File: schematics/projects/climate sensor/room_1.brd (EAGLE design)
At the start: 100 x 80 mm, 8 parts

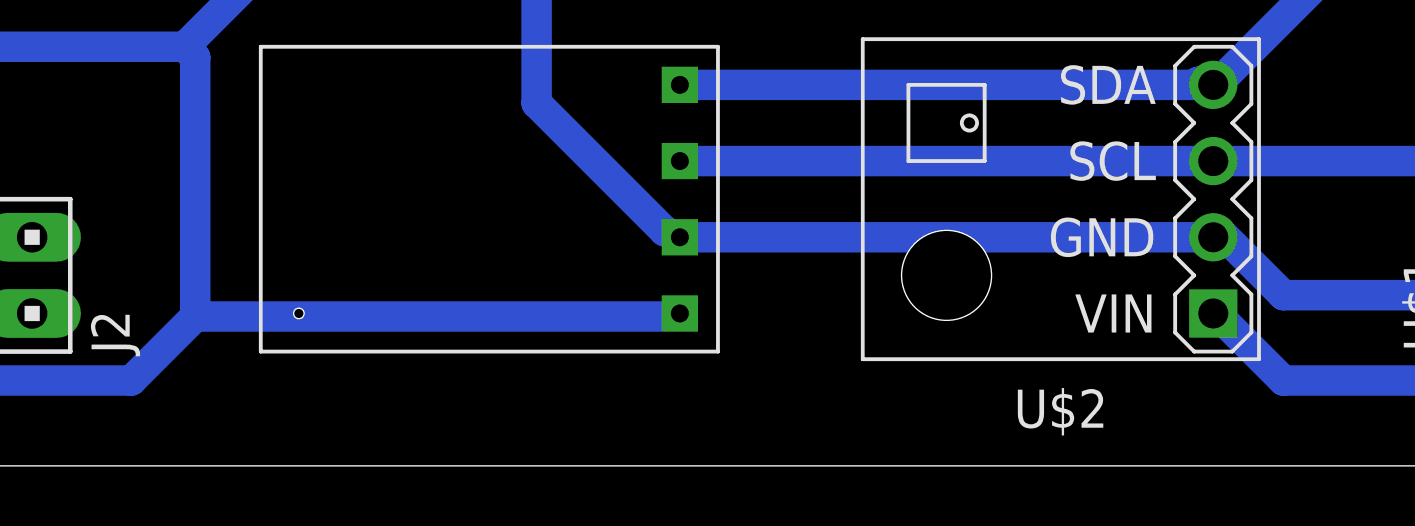
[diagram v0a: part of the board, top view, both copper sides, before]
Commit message: added eagle board files for low-voltage schemas
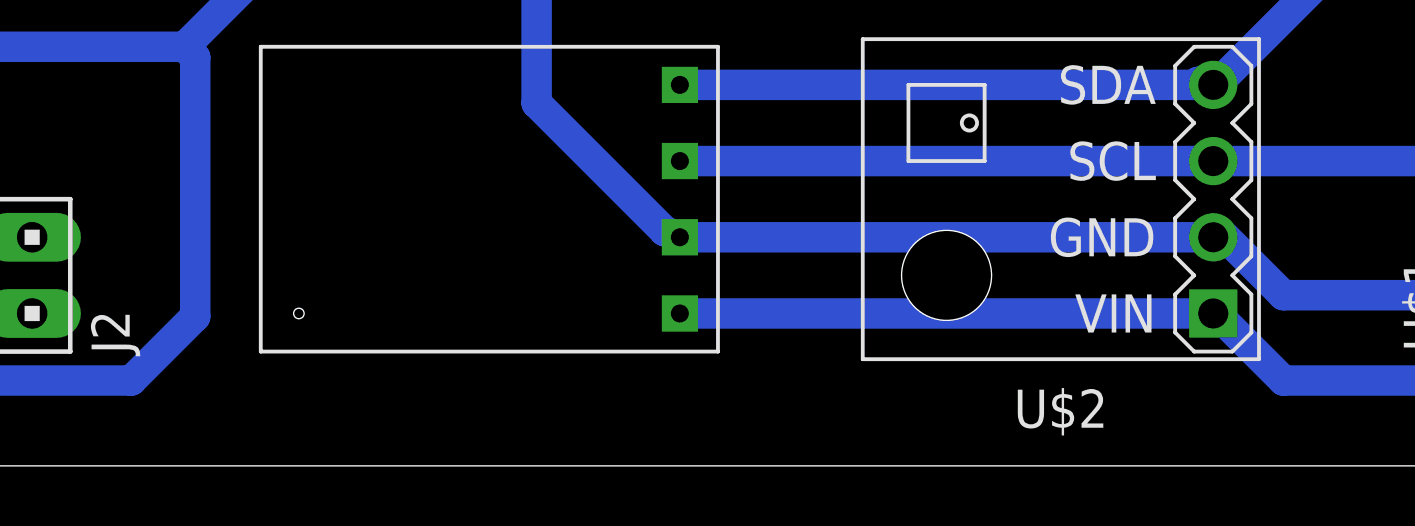
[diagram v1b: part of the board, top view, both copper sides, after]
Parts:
- renumbered GY_SGP1 to GY_SGP30_1
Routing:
- net 3V3: track 114.2 -> 132.2 mm
- net +5V: track 241.8 -> 226.2 mm
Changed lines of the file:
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@@
 <elements>
 <element name="C1" library="my_devices" package="C" value="1000 mF" x="13.97" y="6.35" smashed="yes" rot="R270"/>
-<element name="GY_SGP1" library="my_devices" package="GY-SGP30" value="GY-SGP30" x="43.18" y="8.89" smashed="yes" rot="R180"/>
+<element name="GY_SGP30_1" library="my_devices" package="GY-SGP30" value="GY-SGP30" x="43.18" y="8.89" smashed="yes" rot="R180"/>
 <element name="J2" library="con-amp" library_urn="urn:adsk.eagle:library:127" package="10X02MTA" package3d_urn="urn:adsk.eagle:package:8081649/1" value="" x="21.59" y="6.35" smashed="yes" rot="R90">
 <attribute name="NAME" x="24.8412" y="3.7338" size="1.27" layer="25" rot="R90"/>
@@
 <contactref element="U$3" pad="GND"/>
 <contactref element="U$3" pad="GND_1"/>
-<contactref element="GY_SGP1" pad="GND"/>
+<contactref element="GY_SGP30_1" pad="GND"/>
 <contactref element="U$11" pad="GND"/>
 <contactref element="U$2" pad="2"/>
@@
 <wire x1="93.8784" y1="51.2064" x2="93.97" y2="50.79" width="1.016" layer="16"/>
 <wire x1="27.0256" y1="4.9784" x2="24.892" y2="2.8448" width="1.016" layer="16"/>
-<wire x1="42.672" y1="4.9784" x2="27.0256" y2="4.9784" width="1.016" layer="16"/>
 <wire x1="9.2456" y1="13.97" x2="26.67" y2="13.97" width="1.016" layer="16"/>
 <wire x1="26.67" y1="13.97" x2="27.0256" y2="13.6144" width="1.016" layer="16"/>
@@
 <signal name="I2C_SCL">
 <contactref element="U$1" pad="36"/>
-<contactref element="GY_SGP1" pad="SCL"/>
+<contactref element="GY_SGP30_1" pad="SCL"/>
 <contactref element="U$2" pad="3"/>
 <wire x1="43.18" y1="10.16" x2="60.96" y2="10.16" width="1.016" layer="16"/>
@@
 <signal name="I2C_SDA">
 <contactref element="U$1" pad="33"/>
-<contactref element="GY_SGP1" pad="SDA"/>
+<contactref element="GY_SGP30_1" pad="SDA"/>
 <contactref element="U$2" pad="4"/>
 <wire x1="60.452" y1="12.8016" x2="60.96" y2="12.7" width="1.016" layer="16"/>
@@
 <wire x1="92.1004" y1="6.7564" x2="88.1888" y2="2.8448" width="1.016" layer="16"/>
 <wire x1="61.1632" y1="4.9784" x2="60.96" y2="5.08" width="1.016" layer="16"/>
-<contactref element="GY_SGP1" pad="VIN"/>
-<wire x1="43.18" y1="5.08" x2="60.96" y2="5.08" width="0" layer="19" extent="1-1"/>
+<contactref element="GY_SGP30_1" pad="VIN"/>
+<wire x1="43.18" y1="5.08" x2="61.0616" y2="5.08" width="1.016" layer="16"/>
+<wire x1="61.0616" y1="5.08" x2="61.1632" y2="4.9784" width="1.016" layer="16"/>
 </signal>
 <signal name="UART_0_TXD">

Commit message: changes in board files.
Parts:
- moved J2 2.54 mm to (19.1, 6.35)
- moved C1 1.27 mm to (12.7, 6.35)
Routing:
- net GND: track 125.7 -> 123.1 mm
- net +5V: track 226.2 -> 223.6 mm
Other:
- board text added: "+5V GND"
- board text added: "SUPPLY"
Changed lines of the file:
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@@
 <wire x1="100" y1="80" x2="0" y2="80" width="0" layer="20"/>
 <wire x1="0" y1="80" x2="0" y2="0" width="0" layer="20"/>
+<text x="16.51" y="10.16" size="1.778" layer="1">SUPPLY</text>
+<text x="22.86" y="3.81" size="1.778" layer="1">+5V
+GND</text>
 </plain>
 <attributes>
@@
 </autorouter>
 <elements>
-<element name="C1" library="my_devices" package="C" value="1000 mF" x="13.97" y="6.35" smashed="yes" rot="R270"/>
+<element name="C1" library="my_devices" package="C" value="1000 mF" x="12.7" y="6.35" smashed="yes" rot="R270"/>
 <element name="GY_SGP30_1" library="my_devices" package="GY-SGP30" value="GY-SGP30" x="43.18" y="8.89" smashed="yes" rot="R180"/>
-<element name="J2" library="con-amp" library_urn="urn:adsk.eagle:library:127" package="10X02MTA" package3d_urn="urn:adsk.eagle:package:8081649/1" value="" x="21.59" y="6.35" smashed="yes" rot="R90">
-<attribute name="NAME" x="24.8412" y="3.7338" size="1.27" layer="25" rot="R90"/>
-<attribute name="POPULARITY" value="5" x="74.93" y="52.07" size="1.778" layer="27" rot="R90" display="off"/>
-<attribute name="VALUE" x="19.4391" y="3.8039" size="1.27" layer="27" rot="R90"/>
+<element name="J2" library="con-amp" library_urn="urn:adsk.eagle:library:127" package="10X02MTA" package3d_urn="urn:adsk.eagle:package:8081649/1" value="" x="19.05" y="6.35" smashed="yes" rot="R90">
+<attribute name="NAME" x="22.3012" y="3.7338" size="1.27" layer="25" rot="R90"/>
+<attribute name="POPULARITY" value="5" x="72.39" y="52.07" size="1.778" layer="27" rot="R90" display="off"/>
+<attribute name="VALUE" x="16.8991" y="3.8039" size="1.27" layer="27" rot="R90"/>
 </element>
 <element name="R1" library="my_devices" package="R" value="600" x="55.88" y="40.64" smashed="yes" rot="R270">
@@
 <wire x1="35.56" y1="33.4264" x2="35.56" y2="33.02" width="1.016" layer="16"/>
 <wire x1="43.18" y1="7.62" x2="60.96" y2="7.62" width="1.016" layer="16"/>
-<wire x1="7.7216" y1="5.08" x2="21.59" y2="5.08" width="1.016" layer="16"/>
-<wire x1="6.4008" y1="6.4008" x2="7.7216" y2="5.08" width="1.016" layer="16"/>
-<wire x1="21.59" y1="5.08" x2="13.97" y2="5.08" width="0" layer="19" extent="1-1"/>
+<wire x1="7.7216" y1="5.08" x2="6.4008" y2="6.4008" width="1.016" layer="16"/>
+<wire x1="19.05" y1="5.08" x2="12.7" y2="5.08" width="1.016" layer="16"/>
+<wire x1="12.7" y1="5.08" x2="7.7216" y2="5.08" width="1.016" layer="16"/>
 </signal>
 <signal name="+5V">
@@
 <wire x1="9.2456" y1="13.97" x2="9.2456" y2="19.2024" width="1.016" layer="16"/>
 <wire x1="9.2456" y1="19.2024" x2="8.89" y2="19.05" width="1.016" layer="16"/>
-<wire x1="9.2456" y1="7.8232" x2="14.0208" y2="7.8232" width="1.016" layer="16"/>
-<wire x1="21.9456" y1="7.8232" x2="21.59" y2="7.62" width="1.016" layer="16"/>
-<wire x1="14.0208" y1="7.8232" x2="21.9456" y2="7.8232" width="1.016" layer="16"/>
-<wire x1="14.0208" y1="7.8232" x2="13.97" y2="7.62" width="1.016" layer="16"/>
+<wire x1="9.2456" y1="7.8232" x2="12.7508" y2="7.8232" width="1.016" layer="16"/>
+<wire x1="19.4056" y1="7.8232" x2="19.05" y2="7.62" width="1.016" layer="16"/>
+<wire x1="12.7508" y1="7.8232" x2="19.4056" y2="7.8232" width="1.016" layer="16"/>
+<wire x1="12.7508" y1="7.8232" x2="12.7" y2="7.62" width="1.016" layer="16"/>
 <wire x1="30.5816" y1="32.7152" x2="30.48" y2="33.02" width="1.016" layer="16"/>
 <wire x1="80.3656" y1="51.2064" x2="93.8784" y2="51.2064" width="1.016" layer="16"/>
@@
 </drawing>
 <compatibility>
+<note version="6.3" minversion="6.2.2" severity="warning">
+Since Version 6.2.2 text objects can contain more than one line,
+which will not be processed correctly with this version.
+</note>
 <note version="8.2" severity="warning">
 Since Version 8.2, EAGLE supports online libraries. The ids

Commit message: actualized schematics
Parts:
- moved C1 4.58 mm to (8.89, 8.89)
- moved R1 1.27 mm to (55.9, 41.9)
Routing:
- net N$8: track 20.6 -> 16.5 mm
- net 3V3: track 132.2 -> 135.5 mm
- net GND: track 123.1 -> 122.5 mm
- net +5V: track 223.6 -> 223.1 mm
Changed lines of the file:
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@@
 </autorouter>
 <elements>
-<element name="C1" library="my_devices" package="C" value="1000 mF" x="12.7" y="6.35" smashed="yes" rot="R270"/>
+<element name="C1" library="my_devices" package="C" value="1000 mF" x="8.89" y="8.89" smashed="yes" rot="R270"/>
 <element name="GY_SGP30_1" library="my_devices" package="GY-SGP30" value="GY-SGP30" x="43.18" y="8.89" smashed="yes" rot="R180"/>
 <element name="J2" library="con-amp" library_urn="urn:adsk.eagle:library:127" package="10X02MTA" package3d_urn="urn:adsk.eagle:package:8081649/1" value="" x="19.05" y="6.35" smashed="yes" rot="R90">
@@
 <attribute name="VALUE" x="16.8991" y="3.8039" size="1.27" layer="27" rot="R90"/>
 </element>
-<element name="R1" library="my_devices" package="R" value="600" x="55.88" y="40.64" smashed="yes" rot="R270">
-<attribute name="R" value="" x="-6.35" y="19.05" size="1.778" layer="27" rot="R270" display="off"/>
+<element name="R1" library="my_devices" package="R" value="600" x="55.88" y="41.91" smashed="yes" rot="R270">
+<attribute name="R" value="" x="-6.35" y="20.32" size="1.778" layer="27" rot="R270" display="off"/>
 </element>
 <element name="U$1" library="ESP32-DEVKITC" package="ESP32-DEVKITC" value="ESP32DEVKITC" x="82.55" y="27.94" smashed="yes" rot="R90">
@@
 <contactref element="U$2" pad="2"/>
 <wire x1="6.4008" y1="19.2024" x2="8.5344" y2="21.336" width="1.016" layer="16"/>
-<wire x1="6.4008" y1="19.2024" x2="6.4008" y2="6.4008" width="1.016" layer="16"/>
 <wire x1="8.5344" y1="21.336" x2="8.89" y2="21.59" width="1.016" layer="16"/>
 <wire x1="37.6936" y1="33.4264" x2="35.56" y2="33.4264" width="1.016" layer="16"/>
@@
 <wire x1="35.56" y1="33.4264" x2="35.56" y2="33.02" width="1.016" layer="16"/>
 <wire x1="43.18" y1="7.62" x2="60.96" y2="7.62" width="1.016" layer="16"/>
-<wire x1="7.7216" y1="5.08" x2="6.4008" y2="6.4008" width="1.016" layer="16"/>
-<wire x1="19.05" y1="5.08" x2="12.7" y2="5.08" width="1.016" layer="16"/>
-<wire x1="12.7" y1="5.08" x2="7.7216" y2="5.08" width="1.016" layer="16"/>
+<wire x1="19.05" y1="5.08" x2="8.89" y2="5.08" width="1.016" layer="16"/>
+<wire x1="8.89" y1="5.08" x2="6.4008" y2="7.5692" width="1.016" layer="16"/>
+<wire x1="6.4008" y1="7.5692" x2="6.4008" y2="19.2024" width="1.016" layer="16"/>
 </signal>
 <signal name="+5V">
@@
 <wire x1="30.5816" y1="33.4264" x2="30.48" y2="33.02" width="1.016" layer="16"/>
 <wire x1="32.7152" y1="33.4264" x2="33.02" y2="33.02" width="1.016" layer="16"/>
-<wire x1="9.2456" y1="7.8232" x2="9.2456" y2="13.97" width="1.016" layer="16"/>
-<wire x1="9.2456" y1="13.97" x2="9.2456" y2="19.2024" width="1.016" layer="16"/>
 <wire x1="9.2456" y1="19.2024" x2="8.89" y2="19.05" width="1.016" layer="16"/>
-<wire x1="9.2456" y1="7.8232" x2="12.7508" y2="7.8232" width="1.016" layer="16"/>
 <wire x1="19.4056" y1="7.8232" x2="19.05" y2="7.62" width="1.016" layer="16"/>
-<wire x1="12.7508" y1="7.8232" x2="19.4056" y2="7.8232" width="1.016" layer="16"/>
-<wire x1="12.7508" y1="7.8232" x2="12.7" y2="7.62" width="1.016" layer="16"/>
 <wire x1="30.5816" y1="32.7152" x2="30.48" y2="33.02" width="1.016" layer="16"/>
 <wire x1="80.3656" y1="51.2064" x2="93.8784" y2="51.2064" width="1.016" layer="16"/>
@@
 <wire x1="24.892" y1="2.8448" x2="7.8232" y2="2.8448" width="1.016" layer="16"/>
 <wire x1="93.8784" y1="51.2064" x2="93.97" y2="50.79" width="1.016" layer="16"/>
-<wire x1="27.0256" y1="4.9784" x2="24.892" y2="2.8448" width="1.016" layer="16"/>
-<wire x1="9.2456" y1="13.97" x2="26.67" y2="13.97" width="1.016" layer="16"/>
-<wire x1="26.67" y1="13.97" x2="27.0256" y2="13.6144" width="1.016" layer="16"/>
-<wire x1="27.0256" y1="13.6144" x2="27.0256" y2="4.9784" width="1.016" layer="16"/>
-<wire x1="30.48" y1="33.02" x2="30.48" y2="17.78" width="1.016" layer="16"/>
-<wire x1="30.48" y1="17.78" x2="26.67" y2="13.97" width="1.016" layer="16"/>
+<wire x1="24.892" y1="2.8448" x2="27.0256" y2="4.9784" width="1.016" layer="16"/>
+<wire x1="30.48" y1="17.78" x2="30.48" y2="33.02" width="1.016" layer="16"/>
+<wire x1="27.0256" y1="14.3256" x2="29.21" y2="16.51" width="1.016" layer="16"/>
+<wire x1="29.21" y1="16.51" x2="30.48" y2="17.78" width="1.016" layer="16"/>
+<wire x1="27.0256" y1="4.9784" x2="27.0256" y2="14.3256" width="1.016" layer="16"/>
+<wire x1="19.05" y1="7.62" x2="13.97" y2="7.62" width="1.016" layer="16"/>
+<wire x1="13.97" y1="7.62" x2="8.89" y2="12.7" width="1.016" layer="16"/>
+<wire x1="8.89" y1="12.7" x2="8.89" y2="16.51" width="1.016" layer="16"/>
+<wire x1="8.89" y1="16.51" x2="8.89" y2="19.05" width="1.016" layer="16"/>
+<wire x1="8.89" y1="16.51" x2="29.21" y2="16.51" width="1.016" layer="16"/>
 </signal>
 <signal name="I2C_SCL">
@@
 <contactref element="R1" pad="P$1"/>
 <contactref element="U$2" pad="1"/>
-<wire x1="61.8744" y1="48.3616" x2="56.1848" y2="48.3616" width="1.016" layer="16"/>
-<wire x1="69.6976" y1="56.1848" x2="61.8744" y2="48.3616" width="1.016" layer="16"/>
-<wire x1="73.2536" y1="56.1848" x2="69.6976" y2="56.1848" width="1.016" layer="16"/>
+<wire x1="73.2536" y1="56.1848" x2="69.85" y2="56.1848" width="1.016" layer="16"/>
+<wire x1="69.85" y1="56.1848" x2="69.6976" y2="56.1848" width="1.016" layer="16"/>
 <wire x1="91.7448" y1="37.6936" x2="73.2536" y2="56.1848" width="1.016" layer="16"/>
 <wire x1="91.7448" y1="7.112" x2="91.7448" y2="37.6936" width="1.016" layer="16"/>
 <wire x1="93.8784" y1="4.9784" x2="92.1004" y2="6.7564" width="1.016" layer="16"/>
 <wire x1="92.1004" y1="6.7564" x2="91.7448" y2="7.112" width="1.016" layer="16"/>
-<wire x1="56.1848" y1="48.3616" x2="55.88" y2="48.26" width="1.016" layer="16"/>
 <wire x1="93.8784" y1="4.9784" x2="93.97" y2="5.07" width="1.016" layer="16"/>
 <wire x1="63.2968" y1="2.8448" x2="61.1632" y2="4.9784" width="1.016" layer="16"/>
@@
 <wire x1="43.18" y1="5.08" x2="61.0616" y2="5.08" width="1.016" layer="16"/>
 <wire x1="61.0616" y1="5.08" x2="61.1632" y2="4.9784" width="1.016" layer="16"/>
+<wire x1="52.07" y1="49.53" x2="58.7248" y2="56.1848" width="1.016" layer="16"/>
+<wire x1="58.7248" y1="56.1848" x2="69.6976" y2="56.1848" width="1.016" layer="16"/>
 </signal>
 <signal name="UART_0_TXD">
@@
 <wire x1="40.5384" y1="37.6936" x2="40.5384" y2="33.4264" width="1.016" layer="16"/>
 <wire x1="40.5384" y1="37.6936" x2="40.64" y2="38.1" width="1.016" layer="16"/>
-<wire x1="40.5384" y1="33.4264" x2="55.4736" y2="33.4264" width="1.016" layer="16"/>
-<wire x1="55.4736" y1="33.4264" x2="55.88" y2="33.02" width="1.016" layer="16"/>
 <wire x1="40.5384" y1="33.4264" x2="40.64" y2="33.02" width="1.016" layer="16"/>
+<wire x1="40.64" y1="38.1" x2="52.07" y2="38.1" width="1.016" layer="16"/>
 </signal>
 </signals>
